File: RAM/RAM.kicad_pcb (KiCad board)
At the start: 2 copper layers, 138 x 63.8 mm, 48 parts, among them J1 Conn_01x02_Pin, J2 Conn_01x02_Pin, J3 Conn_01x04_Pin, J4 Conn_01x06_Pin, J5 Conn_01x08_Socket, U2 CD74HCT258E, U3 SN74HCT245N, U4 CD74HCT258E, U6 CD74HCT258E, U7 ATMEGA328-PU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

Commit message: Exposed SPI and RST on atmega chips
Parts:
- added J6: Conn_01x03_Pin, Connector_PinHeader_1.00mm:PinHeader_1x03_P1.00mm_Vertical, F.Cu at (198.5, 50.2)
- added J7: Conn_01x03_Pin, Connector_PinHeader_1.00mm:PinHeader_1x03_P1.00mm_Vertical, F.Cu at (158.5, 50.2)
- added J8: Conn_01x01_Pin, Connector_PinHeader_1.00mm:PinHeader_1x01_P1.00mm_Vertical, F.Cu at (169.5, 64.0)
- added J9: Conn_01x01_Pin, Connector_PinHeader_1.00mm:PinHeader_1x01_P1.00mm_Vertical, F.Cu at (129.5, 64.0)
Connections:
- net Net-(U7-PC6) renamed /AtmegaRamEmulatorA/RST
- net Net-(U8-PC6) renamed /AtmegaRamEmulatorB/RST
- U7 pad 14: unconnected-(U7-PB0-Pad14) -> /AtmegaRamEmulatorA/~{WE}
- U7 pad 17: unconnected-(U7-PB3-Pad17) -> /AtmegaRamEmulatorA/SDO
- U7 pad 18: /AtmegaRamEmulatorA/~{WE} -> /AtmegaRamEmulatorA/SDI
- U7 pad 19: GND -> /AtmegaRamEmulatorA/SCK
- U7 pad 28: unconnected-(U7-PC5-Pad28) -> GND
- U8 pad 14: unconnected-(U8-PB0-Pad14) -> /AtmegaRamEmulatorA/~{WE}
- U8 pad 17: unconnected-(U8-PB3-Pad17) -> /AtmegaRamEmulatorB/SDO
- U8 pad 18: /AtmegaRamEmulatorA/~{WE} -> /AtmegaRamEmulatorB/SDI
- U8 pad 19: GND -> /AtmegaRamEmulatorB/SCK
- U8 pad 28: unconnected-(U8-PC5-Pad28) -> GND
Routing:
- net +5V: track 34.0 -> 68.5 mm
- net /AtmegaRamEmulatorB/SCK: track 0.00 -> 5.32 mm
- net /AtmegaRamEmulatorA/SCK: track 0.00 -> 5.32 mm
- net /AtmegaRamEmulatorB/SDI: track 0.00 -> 3.89 mm
- net /AtmegaRamEmulatorA/SDI: track 0.00 -> 3.89 mm
- net /AtmegaRamEmulatorB/SDO: track 0.00 -> 3.26 mm
- net /AtmegaRamEmulatorA/SDO: track 0.00 -> 3.26 mm
- net /AtmegaRamEmulatorB/RST: track 4.23 -> 7.29 mm
- net /AtmegaRamEmulatorA/RST: track 4.11 -> 7.18 mm
- net /AtmegaRamEmulatorA/~{WE}: track 82.1 -> 80.6 mm
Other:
- board text added: "RST"
- board text added: "SCK"
- board text added: "SDI"
- board text added: "SDO"

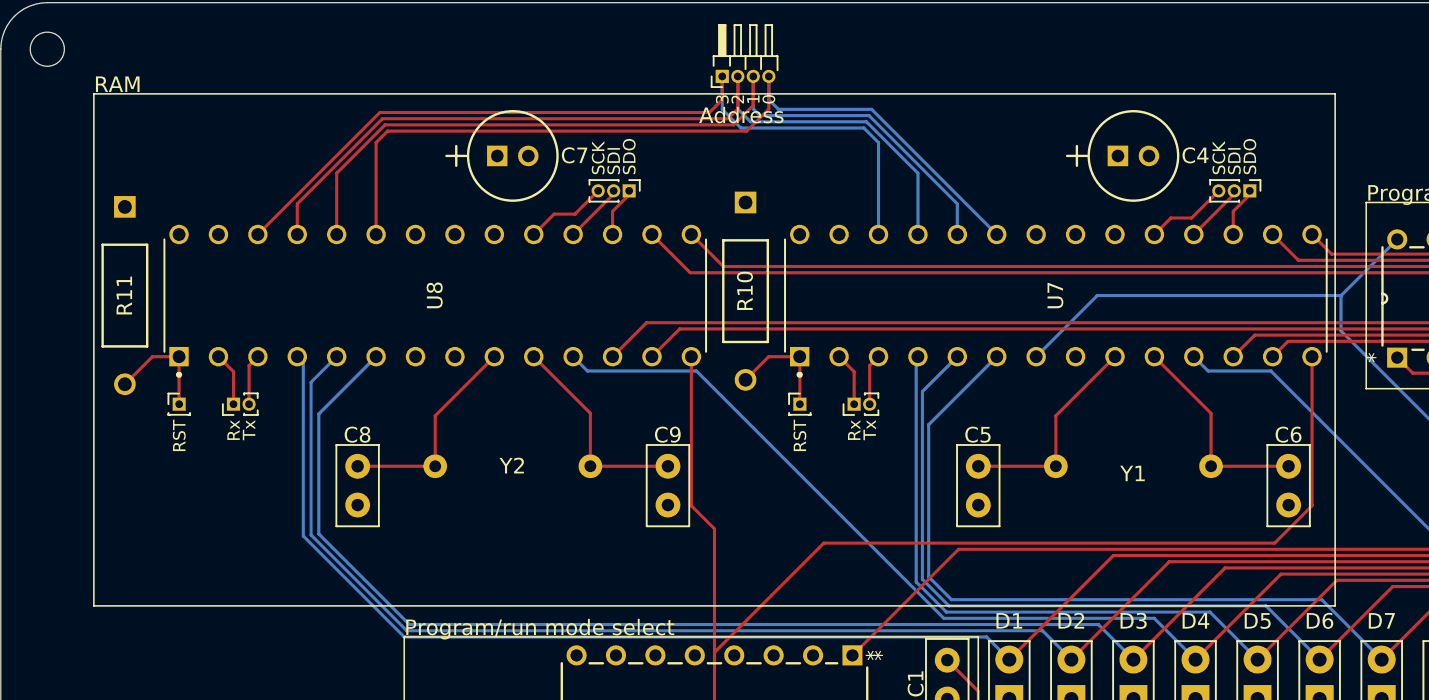
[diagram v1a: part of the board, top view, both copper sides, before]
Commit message: Updated RAM with accurate crystal footprints
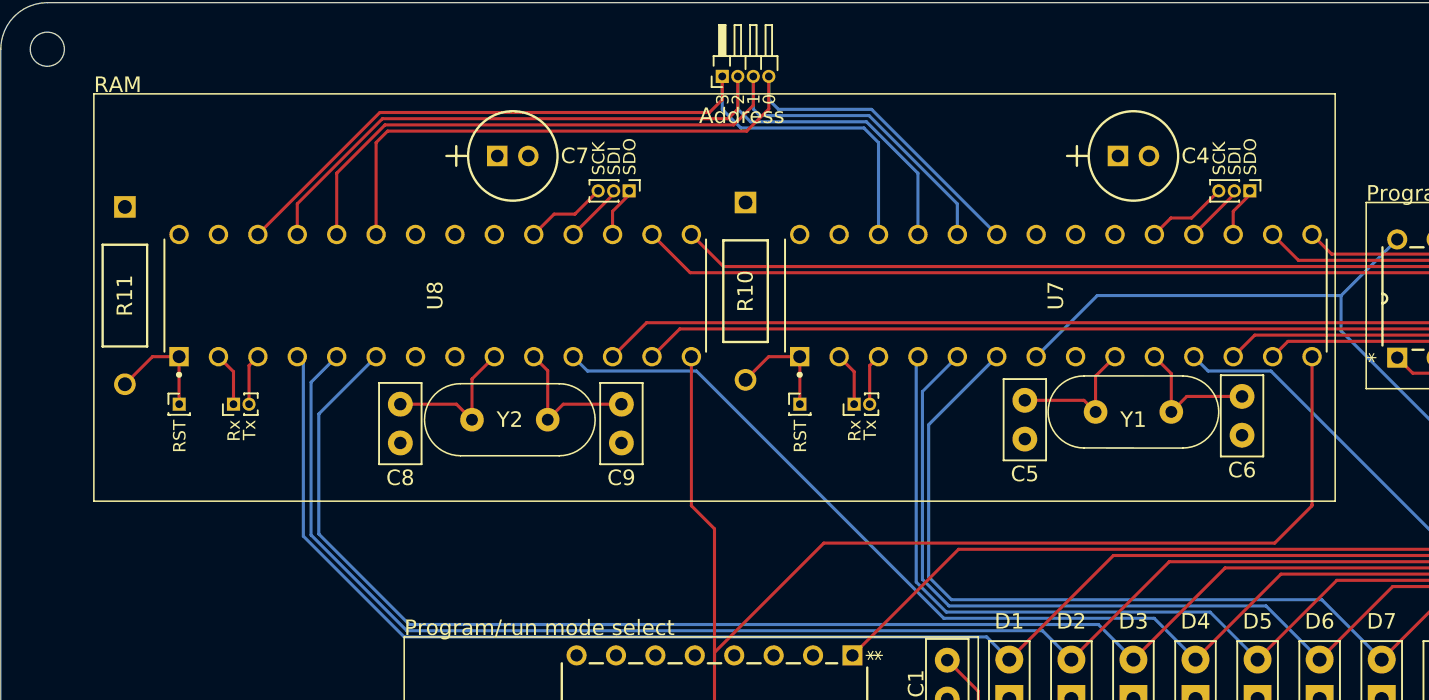
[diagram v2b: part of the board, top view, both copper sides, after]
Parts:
- moved C6 5.41 mm to (198.0, 66.0)
- moved C5 5.20 mm to (184.0, 63.8)
- moved C9 5.00 mm to (158.0, 66.5)
- moved C8 4.85 mm to (143.8, 64.0)
- moved Y1 3.50 mm to (191.0, 64.5)
- moved Y2 3.01 mm to (150.8, 65.0)
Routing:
- net /AtmegaRamEmulatorA/XTAL1: track 13.6 -> 8.95 mm
- net /AtmegaRamEmulatorA/XTAL2: track 13.6 -> 8.99 mm
- net /AtmegaRamEmulatorB/XTAL2: track 13.6 -> 9.60 mm
- net /AtmegaRamEmulatorB/XTAL1: track 13.6 -> 9.69 mm
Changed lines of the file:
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@@
 	(footprint "Capacitor_THT:C_Disc_D5.0mm_W2.5mm_P2.50mm"
 		(layer "F.Cu")
-		(at 181 68 -90)
+		(at 184 63.75 -90)
 		(descr "C, Disc series, Radial, pin pitch=2.50mm, , diameter*width=5*2.5mm^2, Capacitor, http://cdn-reichelt.de/documents/datenblatt/B300/DS_KERKO_TC.pdf")
 		(tags "C Disc series Radial pin pitch 2.50mm  diameter 5mm width 2.5mm Capacitor")
 		(property "Reference" "C5"
-			(at -2 0 180)
+			(at 4.75 0 180)
 			(layer "F.SilkS")
 			(effects
@@
 	(footprint "Capacitor_THT:C_Disc_D5.0mm_W2.5mm_P2.50mm"
 		(layer "F.Cu")
-		(at 161 70.5 90)
+		(at 158 66.5 90)
 		(descr "C, Disc series, Radial, pin pitch=2.50mm, , diameter*width=5*2.5mm^2, Capacitor, http://cdn-reichelt.de/documents/datenblatt/B300/DS_KERKO_TC.pdf")
 		(tags "C Disc series Radial pin pitch 2.50mm  diameter 5mm width 2.5mm Capacitor")
 		(property "Reference" "C9"
-			(at 4.5 0 180)
+			(at -2.25 0 180)
 			(layer "F.SilkS")
 			(effects
@@
 	(footprint "Capacitor_THT:C_Disc_D5.0mm_W2.5mm_P2.50mm"
 		(layer "F.Cu")
-		(at 141 68 -90)
+		(at 143.75 64 -90)
 		(descr "C, Disc series, Radial, pin pitch=2.50mm, , diameter*width=5*2.5mm^2, Capacitor, http://cdn-reichelt.de/documents/datenblatt/B300/DS_KERKO_TC.pdf")
 		(tags "C Disc series Radial pin pitch 2.50mm  diameter 5mm width 2.5mm Capacitor")
 		(property "Reference" "C8"
-			(at -2 0 180)
+			(at 4.75 0 180)
 			(layer "F.SilkS")
 			(effects
@@
 	(footprint "8BitCPUFootprints:16MHzCrystalOscillator"
 		(layer "F.Cu")
-		(at 151 68 180)
+		(at 150.81 65 180)
 		(property "Reference" "Y2"
 			(at 0 0 0)
@@
 		(sheetfile "atmega_ram_emulator.kicad_sch")
 		(attr through_hole)
+		(fp_line
+			(start 3.1775 2.3225)
+			(end -3.175 2.32)
+			(stroke
+				(width 0.1)
+				(type default)
+			)
+			(layer "F.SilkS")
+		)
+		(fp_line
+			(start 3.175 -2.3225)
+			(end -3.175 -2.325)
+			(stroke
+				(width 0.1)
+				(type default)
+			)
+			(layer "F.SilkS")
+		)
+		(fp_arc
+			(start 3.1775 -2.3225)
+			(mid 5.5 0)
+			(end 3.1775 2.3225)
+			(stroke
+				(width 0.1)
+				(type default)
+			)
+			(layer "F.SilkS")
+		)
+		(fp_arc
+			(start -3.175 2.32)
+			(mid -5.4975 -0.0025)
+			(end -3.175 -2.325)
+			(stroke
+				(width 0.1)
+				(type default)
+			)
+			(layer "F.SilkS")
+		)
 		(fp_text user "${REFERENCE}"
 			(at 0 2.5 180)
@@
 		)
 		(pad "1" thru_hole circle
-			(at -5 0 180)
+			(at -2.44 0 180)
 			(size 1.524 1.524)
 			(drill 0.762)
@@
 		)
 		(pad "2" thru_hole circle
-			(at 5 0 180)
+			(at 2.44 0 180)
 			(size 1.524 1.524)
 			(drill 0.762)
@@
 			(polygon
 				(pts
-					(xy 159.25 73.5) (xy 142.75 73.5) (xy 142.75 62.5) (xy 159.25 62.5)
+					(xy 156.31 67.5) (xy 145.31 67.5) (xy 145.31 62.5) (xy 156.31 62.5)
 				)
 			)
@@
 	(footprint "Capacitor_THT:C_Disc_D5.0mm_W2.5mm_P2.50mm"
 		(layer "F.Cu")
-		(at 201 70.5 90)
+		(at 198 66 90)
 		(descr "C, Disc series, Radial, pin pitch=2.50mm, , diameter*width=5*2.5mm^2, Capacitor, http://cdn-reichelt.de/documents/datenblatt/B300/DS_KERKO_TC.pdf")
 		(tags "C Disc series Radial pin pitch 2.50mm  diameter 5mm width 2.5mm Capacitor")
 		(property "Reference" "C6"
-			(at 4.5 0 180)
+			(at -2.25 0 180)
 			(layer "F.SilkS")
 			(effects
@@
 	(footprint "8BitCPUFootprints:16MHzCrystalOscillator"
 		(layer "F.Cu")
-		(at 191 68 180)
+		(at 191 64.5 180)
 		(property "Reference" "Y1"
 			(at 0 -0.5 0)
@@
 		(sheetfile "atmega_ram_emulator.kicad_sch")
 		(attr through_hole)
+		(fp_line
+			(start 3.1775 2.3225)
+			(end -3.175 2.32)
+			(stroke
+				(width 0.1)
+				(type default)
+			)
+			(layer "F.SilkS")
+		)
+		(fp_line
+			(start 3.175 -2.3225)
+			(end -3.175 -2.325)
+			(stroke
+				(width 0.1)
+				(type default)
+			)
+			(layer "F.SilkS")
+		)
+		(fp_arc
+			(start 3.1775 -2.3225)
+			(mid 5.5 0)
+			(end 3.1775 2.3225)
+			(stroke
+				(width 0.1)
+				(type default)
+			)
+			(layer "F.SilkS")
+		)
+		(fp_arc
+			(start -3.175 2.32)
+			(mid -5.4975 -0.0025)
+			(end -3.175 -2.325)
+			(stroke
+				(width 0.1)
+				(type default)
+			)
+			(layer "F.SilkS")
+		)
 		(fp_text user "${REFERENCE}"
 			(at 0 2.5 180)
@@
 		)
 		(pad "1" thru_hole circle
-			(at -5 0 180)
+			(at -2.44 0 180)
 			(size 1.524 1.524)
 			(drill 0.762)
@@
 		)
 		(pad "2" thru_hole circle
-			(at 5 0 180)
+			(at 2.44 0 180)
 			(size 1.524 1.524)
 			(drill 0.762)
@@
 			(polygon
 				(pts
-					(xy 199.25 73.5) (xy 182.75 73.5) (xy 182.75 62.5) (xy 199.25 62.5)
+					(xy 196.5 67) (xy 185.5 67) (xy 185.5 62) (xy 196.5 62)
 				)
 			)
@@
 		)
 		(fp_text user "${REFERENCE}"
-			(at 0 1 360)
+			(at 0 1 0)
 			(layer "F.Fab")
 			(effects
@@
 		)
 		(fp_text user "${REFERENCE}"
-			(at 0 1 360)
+			(at 0 1 0)
 			(layer "F.Fab")
 			(effects
@@
 	(gr_rect
 		(start 124 44)
-		(end 204 77)
+		(end 204 70.25)
 		(stroke
 			(width 0.1)
@@
 	)
 	(segment
-		(start 186 68)
-		(end 181 68)
+		(start 188.56 62.187)
+		(end 189.81 60.937)
 		(width 0.2)
 		(layer "F.Cu")
@@
 	)
 	(segment
-		(start 186 64.747)
-		(end 189.81 60.937)
+		(start 187.81 63.75)
+		(end 188.56 64.5)
+		(width 0.2)
+		(layer "F.Cu")
+		(net 5)
+	)
+	(segment
+		(start 188.56 64.5)
+		(end 188.56 62.187)
 		(width 0.2)
 		(layer "F.Cu")
@@
 	)
 	(segment
-		(start 186 68)
-		(end 186 64.747)
+		(start 184 63.75)
+		(end 187.81 63.75)
 		(width 0.2)
 		(layer "F.Cu")
@@
 	)
 	(segment
-		(start 201 68)
-		(end 196 68)
+		(start 193.44 62.027)
+		(end 193.44 64.5)
 		(width 0.2)
 		(layer "F.Cu")
@@
 	)
 	(segment
-		(start 196 64.587)
-		(end 192.35 60.937)
+		(start 194.44 63.5)
+		(end 193.44 64.5)
 		(width 0.2)
 		(layer "F.Cu")
@@
 	)
 	(segment
-		(start 196 68)
-		(end 196 64.587)
+		(start 198 63.5)
+		(end 194.44 63.5)
 		(width 0.2)
 		(layer "F.Cu")
@@
 	)
 	(segment
-		(start 141 68)
-		(end 146 68)
+		(start 192.35 60.937)
+		(end 193.44 62.027)
 		(width 0.2)
 		(layer "F.Cu")
-		(net 7)
+		(net 6)
 	)
 	(segment
-		(start 146 64.747)
+		(start 148.37 62.377)
 		(end 149.81 60.937)
 		(width 0.2)
@@
 	)
 	(segment
-		(start 146 68)
-		(end 146 64.747)
+		(start 148.37 65)
+		(end 148.37 62.377)
+		(width 0.2)
+		(layer "F.Cu")
+		(net 7)
+	)
+	(segment
+		(start 143.75 64)
+		(end 147.37 64)
 		(width 0.2)
 		(layer "F.Cu")
@@
 	)
 	(segment
-		(start 156 68)
-		(end 161 68)
+		(start 147.37 64)
+		(end 148.37 65)
+		(width 0.2)
+		(layer "F.Cu")
+		(net 7)
+	)
+	(segment
+		(start 154.25 64)
+		(end 153.25 65)
+		(width 0.2)
+		(layer "F.Cu")
+		(net 8)
+	)
+	(segment
+		(start 153.25 65)
+		(end 153.25 61.837)
 		(width 0.2)
 		(layer "F.Cu")
@@
 	)
 	(segment
-		(start 156 68)
-		(end 156 64.587)
+		(start 158 64)
+		(end 154.25 64)
 		(width 0.2)
 		(layer "F.Cu")
@@
 	)
 	(segment
-		(start 156 64.587)
+		(start 153.25 61.837)
 		(end 152.35 60.937)
 		(width 0.2)

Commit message: Updated RAM push button to use pins that aren't shorted together
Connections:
- S1 pad 2: GND -> (no net)
- S1 pad 4: (no net) -> GND
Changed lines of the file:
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@@
 			(layers "*.Cu" "*.Mask")
 			(remove_unused_layers no)
-			(net 4 "GND")
-			(pintype "passive")
 			(solder_mask_margin 0.102)
 		)
@@
 			(layers "*.Cu" "*.Mask")
 			(remove_unused_layers no)
+			(net 4 "GND")
+			(pintype "passive")
 			(solder_mask_margin 0.102)
 		)

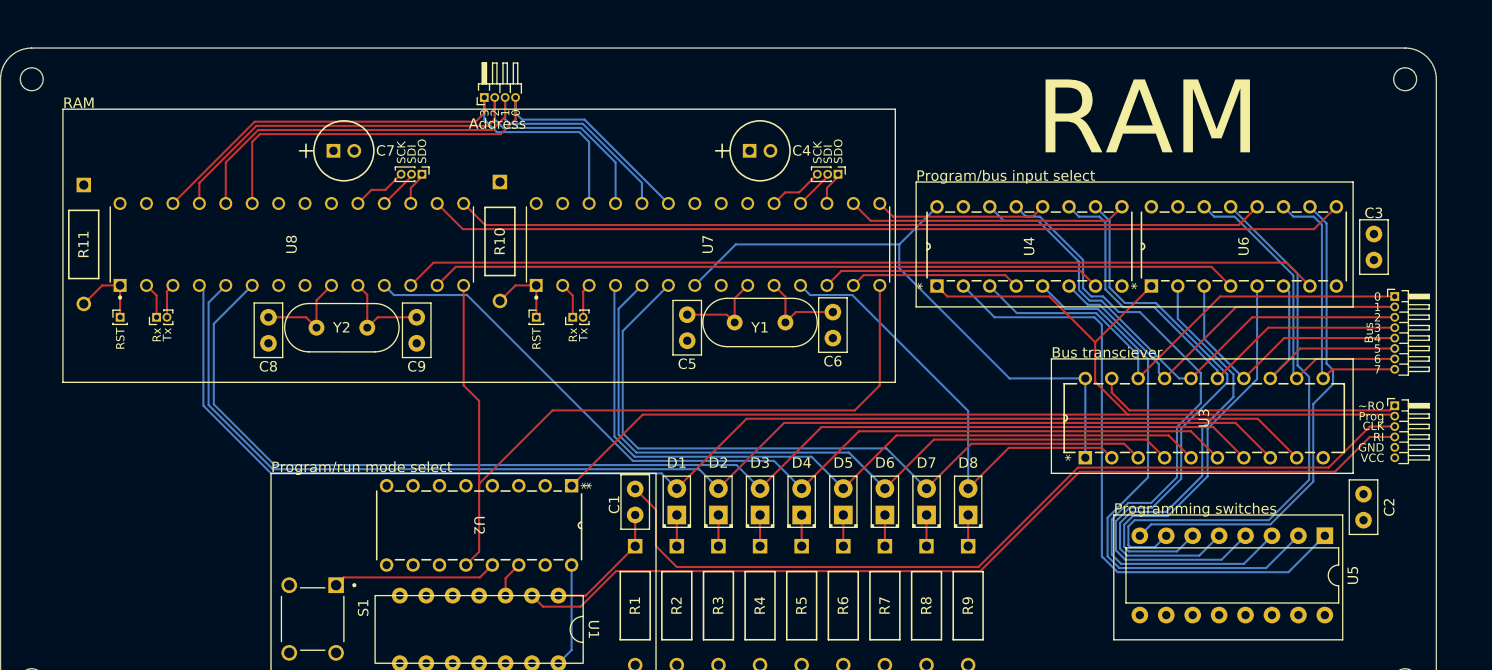
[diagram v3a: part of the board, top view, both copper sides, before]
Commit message: Updated RAM pin headers to 2.54mm and correct assignment
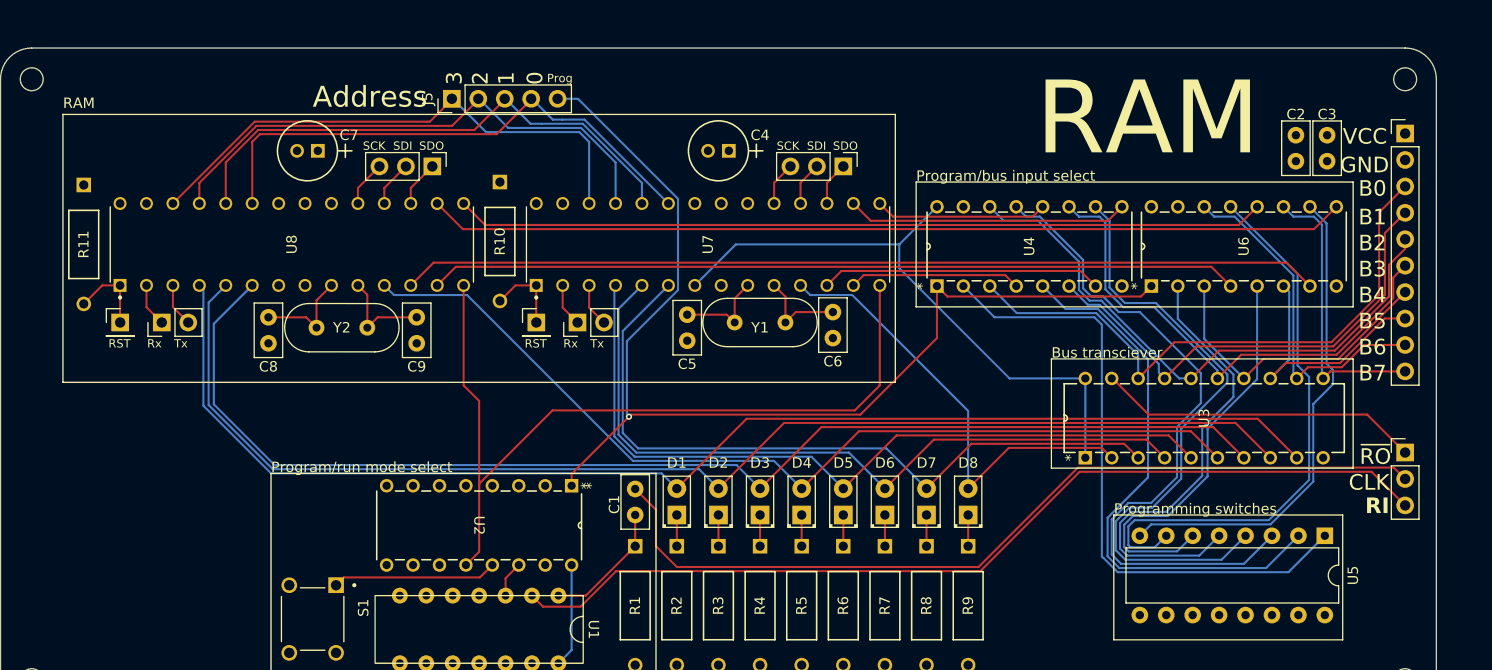
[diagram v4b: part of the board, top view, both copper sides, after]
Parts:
- removed the J3 at (164.5, 42.9)
- removed the J4 at (252.0, 72.5)
- added J8: Conn_01x03_Pin, Connector_PinHeader_2.54mm:PinHeader_1x03_P2.54mm_Vertical, F.Cu at (253.0, 77.0)
- added J9: Conn_01x10_Pin, Connector_PinHeader_2.54mm:PinHeader_1x10_P2.54mm_Vertical, F.Cu at (253.0, 46.3)
- J1: footprint Connector_PinHeader_1.00mm:PinHeader_1x02_P1.00mm_Vertical -> Connector_PinHeader_2.54mm:PinHeader_1x02_P2.54mm_Vertical
- J2: renamed from J8; footprint Connector_PinHeader_1.00mm:PinHeader_1x01_P1.00mm_Vertical -> Connector_PinHeader_2.54mm:PinHeader_1x01_P2.54mm_Vertical
- J3: renamed from J2; footprint Connector_PinHeader_1.00mm:PinHeader_1x02_P1.00mm_Vertical -> Connector_PinHeader_2.54mm:PinHeader_1x02_P2.54mm_Vertical
- J4: renamed from J9; footprint Connector_PinHeader_1.00mm:PinHeader_1x01_P1.00mm_Vertical -> Connector_PinHeader_2.54mm:PinHeader_1x01_P2.54mm_Vertical
- J5: value Conn_01x08_Socket -> Conn_01x05_Pin; footprint Connector_PinHeader_1.00mm:PinHeader_1x08_P1.00mm_Horizontal -> Connector_PinHeader_2.54mm:PinHeader_1x05_P2.54mm_Vertical
- J6, J7: footprint Connector_PinHeader_1.00mm:PinHeader_1x03_P1.00mm_Vertical -> Connector_PinHeader_2.54mm:PinHeader_1x03_P2.54mm_Vertical
- moved J5 92.6 mm to (161.4, 43.0), turned to 90 degrees
- moved C2 35.1 mm to (242.5, 46.5)
- moved C3 12.8 mm to (245.5, 46.5), turned to -90 degrees
- moved C4 2.00 mm to (188.0, 48.0), turned to 180 degrees
- moved C7 1.50 mm to (148.5, 48.0), turned to 180 degrees
- moved J7 1.25 mm to (159.5, 49.5)
- moved J6 0.90 mm to (199.0, 49.5)
- moved J3 0.71 mm to (133.5, 64.5)
- moved J1 0.68 mm to (173.5, 64.5)
- moved J2 0.50 mm to (169.5, 64.5)
- moved J4 0.50 mm to (129.5, 64.5)
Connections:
- J5 pad 1: /Bus 0 -> /A3
- J5 pad 2: /Bus 1 -> /A2
- J5 pad 3: /Bus 2 -> /A1
- J5 pad 4: /Bus 3 -> /A0
- J5 pad 5: /Bus 4 -> /Program
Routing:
- net /Bus 0: track 47.2 -> 57.2 mm
- net /Program: track 115.3 -> 106.7 mm, vias 0 -> 1
- net /Bus 1: track 38.3 -> 46.5 mm
- net /Bus 2: track 49.8 -> 56.2 mm
- net /Bus 3: track 44.4 -> 49.0 mm
- net /Bus 4: track 26.6 -> 29.4 mm
- net /A2: track 54.4 -> 51.8 mm
- net /A1: track 54.2 -> 51.8 mm
- net /A3: track 54.0 -> 51.8 mm
- net /A0: track 54.0 -> 51.8 mm
- net /Bus 5: track 23.0 -> 25.2 mm
- net /~Read out: track 29.5 -> 31.1 mm
- net /Bus 6: track 31.5 -> 33.1 mm
- net /AtmegaRamEmulatorB/SDO: track 3.26 -> 4.42 mm
- net /AtmegaRamEmulatorA/SCK: track 5.32 -> 4.21 mm
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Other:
- board text added: "B0"
- board text added: "B1"
- board text added: "B2"
- board text added: "B3"
- board text added: "B4"
- board text added: "B5"
- board text added: "B6"
- board text added: "B7"
- board text added: "~{RO}"
- board text removed: "4"
- board text removed: "5"
- board text removed: "6"
- board text removed: "7"
- board text removed: "Bus"
- board text removed: "TODO: Update crystal footprint"
- board text removed: "~RO"
